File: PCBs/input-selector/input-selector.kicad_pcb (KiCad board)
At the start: 2 copper layers, 90.2 x 52.1 mm, 46 parts, among them J1 Conn_01x06_Male, K1 IM40, K2 IM40, K3 IM40, K4 IM40, K5 IM40, K6 IM40, U1 ULN2003, U2 MCP23S17_SO, U3 ULN2003

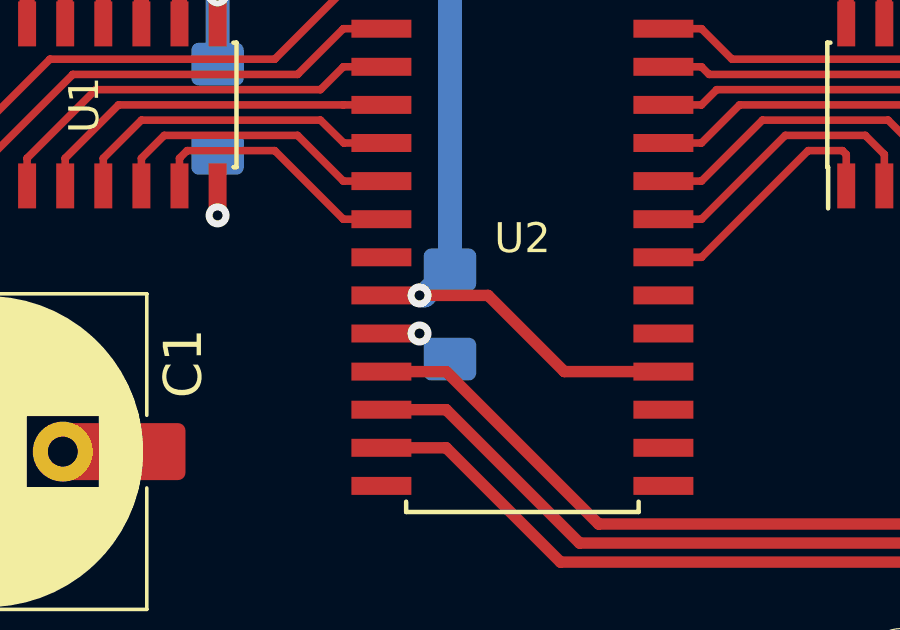
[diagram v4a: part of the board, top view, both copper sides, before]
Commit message: adding BoMs, images and small design updates
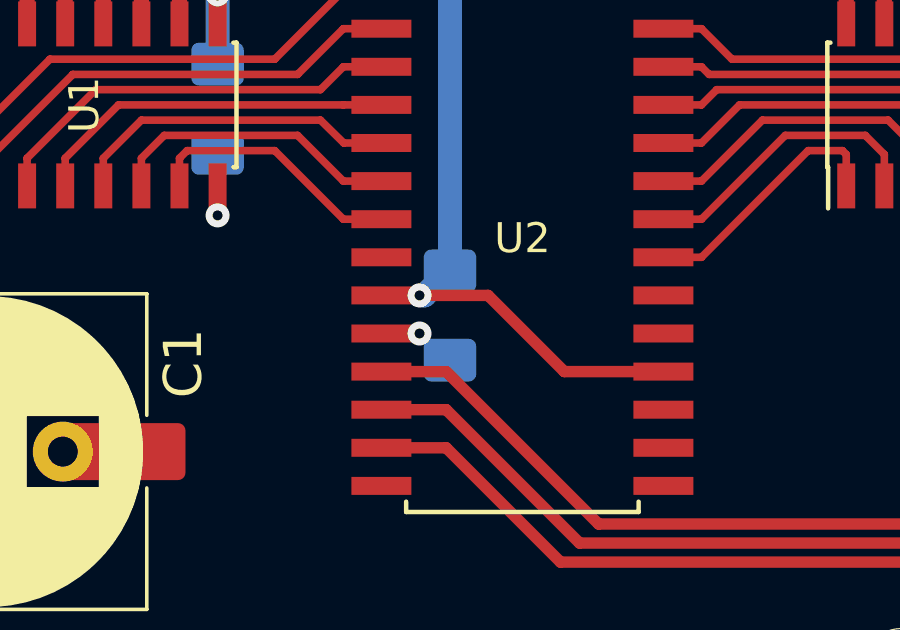
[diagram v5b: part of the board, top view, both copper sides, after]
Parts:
- removed C1: C, Capacitor_SMD:C_1206_3216Metric_Pad1.42x1.75mm_HandSolder
- added C4: C, Capacitor_SMD:C_1206_3216Metric_Pad1.42x1.75mm_HandSolder, B.Cu at (125.2, 106.7)
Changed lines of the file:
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@@
     (add_net "Net-(U2-Pad8)")
+  )
+  (module Capacitor_SMD:C_1206_3216Metric_Pad1.42x1.75mm_HandSolder (layer B.Cu)
+    (at 125.222 106.7165 270)
+    (descr "Capacitor SMD 1206 (3216 Metric), square (rectangular) end terminal, IPC_7351 nominal with elongated pad for handsoldering. (Body size source: http://www.tortai-tech.com/upload/download/2011102023233369053.pdf), generated with kicad-footprint-generator")
+    (tags "capacitor handsolder")
+    (attr smd)
+    (fp_text reference C4 (at 0 1.82 270) (layer B.SilkS)
+      (effects (font (size 1 1) (thickness 0.15)) (justify mirror))
+    )
+    (fp_text value C (at 0 -1.82 270) (layer B.Fab)
+      (effects (font (size 1 1) (thickness 0.15)) (justify mirror))
+    )
+    (fp_line (start -1.6 -0.8) (end -1.6 0.8) (layer B.Fab) (width 0.1))
+    (fp_line (start -1.6 0.8) (end 1.6 0.8) (layer B.Fab) (width 0.1))
+    (fp_line (start 1.6 0.8) (end 1.6 -0.8) (layer B.Fab) (width 0.1))
+    (fp_line (start 1.6 -0.8) (end -1.6 -0.8) (layer B.Fab) (width 0.1))
+    (fp_line (start -0.602064 0.91) (end 0.602064 0.91) (layer B.SilkS) (width 0.12))
+    (fp_line (start -0.602064 -0.91) (end 0.602064 -0.91) (layer B.SilkS) (width 0.12))
+    (fp_line (start -2.45 -1.12) (end -2.45 1.12) (layer B.CrtYd) (width 0.05))
+    (fp_line (start -2.45 1.12) (end 2.45 1.12) (layer B.CrtYd) (width 0.05))
+    (fp_line (start 2.45 1.12) (end 2.45 -1.12) (layer B.CrtYd) (width 0.05))
+    (fp_line (start 2.45 -1.12) (end -2.45 -1.12) (layer B.CrtYd) (width 0.05))
+    (fp_text user %R (at 0 0 270) (layer B.Fab)
+      (effects (font (size 0.8 0.8) (thickness 0.12)) (justify mirror))
+    )
+    (pad 1 smd roundrect (at -1.4875 0 270) (size 1.425 1.75) (layers B.Cu B.Paste B.Mask) (roundrect_rratio 0.175439)
+      (net 65 VDD))
+    (pad 2 smd roundrect (at 1.4875 0 270) (size 1.425 1.75) (layers B.Cu B.Paste B.Mask) (roundrect_rratio 0.175439)
+      (net 67 GND))
+    (model ${KISYS3DMOD}/Capacitor_SMD.3dshapes/C_1206_3216Metric.wrl
+      (at (xyz 0 0 0))
+      (scale (xyz 1 1 1))
+      (rotate (xyz 0 0 0))
+    )
   )
   (module omron-relay:g6j-2p-y (layer F.Cu)
@@
       (at (xyz 0 0 0))
       (scale (xyz 1 1 1))
-      (rotate (xyz 0 0 0))
-    )
-  )
-  (module Capacitor_SMD:C_1206_3216Metric_Pad1.42x1.75mm_HandSolder (layer B.Cu)
-    (at 125.222 106.68 270)
-    (descr "Capacitor SMD 1206 (3216 Metric), square (rectangular) end terminal, IPC_7351 nominal with elongated pad for handsoldering. (Body size source: http://www.tortai-tech.com/upload/download/2011102023233369053.pdf), generated with kicad-footprint-generator")
-    (tags "capacitor handsolder")
-    (attr smd)
-    (fp_text reference C1 (at 0 1.82 270) (layer B.SilkS)
-      (effects (font (size 1 1) (thickness 0.15)) (justify mirror))
-    )
-    (fp_text value C (at 0 -1.82 270) (layer B.Fab)
-      (effects (font (size 1 1) (thickness 0.15)) (justify mirror))
-    )
-    (fp_text user %R (at 0 0 270) (layer B.Fab)
-      (effects (font (size 0.8 0.8) (thickness 0.12)) (justify mirror))
-    )
-    (fp_line (start 2.45 -1.12) (end -2.45 -1.12) (layer B.CrtYd) (width 0.05))
-    (fp_line (start 2.45 1.12) (end 2.45 -1.12) (layer B.CrtYd) (width 0.05))
-    (fp_line (start -2.45 1.12) (end 2.45 1.12) (layer B.CrtYd) (width 0.05))
-    (fp_line (start -2.45 -1.12) (end -2.45 1.12) (layer B.CrtYd) (width 0.05))
-    (fp_line (start -0.602064 -0.91) (end 0.602064 -0.91) (layer B.SilkS) (width 0.12))
-    (fp_line (start -0.602064 0.91) (end 0.602064 0.91) (layer B.SilkS) (width 0.12))
-    (fp_line (start 1.6 -0.8) (end -1.6 -0.8) (layer B.Fab) (width 0.1))
-    (fp_line (start 1.6 0.8) (end 1.6 -0.8) (layer B.Fab) (width 0.1))
-    (fp_line (start -1.6 0.8) (end 1.6 0.8) (layer B.Fab) (width 0.1))
-    (fp_line (start -1.6 -0.8) (end -1.6 0.8) (layer B.Fab) (width 0.1))
-    (pad 2 smd roundrect (at 1.4875 0 270) (size 1.425 1.75) (layers B.Cu B.Paste B.Mask) (roundrect_rratio 0.175439)
-      (net 67 GND))
-    (pad 1 smd roundrect (at -1.4875 0 270) (size 1.425 1.75) (layers B.Cu B.Paste B.Mask) (roundrect_rratio 0.175439)
-      (net 65 VDD))
-    (model ${KISYS3DMOD}/Capacitor_SMD.3dshapes/C_1206_3216Metric.wrl
-      (at (xyz 0 0 0))
-      (scale (xyz 1 1 1))
